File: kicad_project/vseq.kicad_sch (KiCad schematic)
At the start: 47 parts, among them J1 STM32_ADC_IN, J2 PROBE_INPUTS, U1 MCP6002, U2 MCP6002, U3 MCP6002, U4 MCP6002, U5 MCP6002

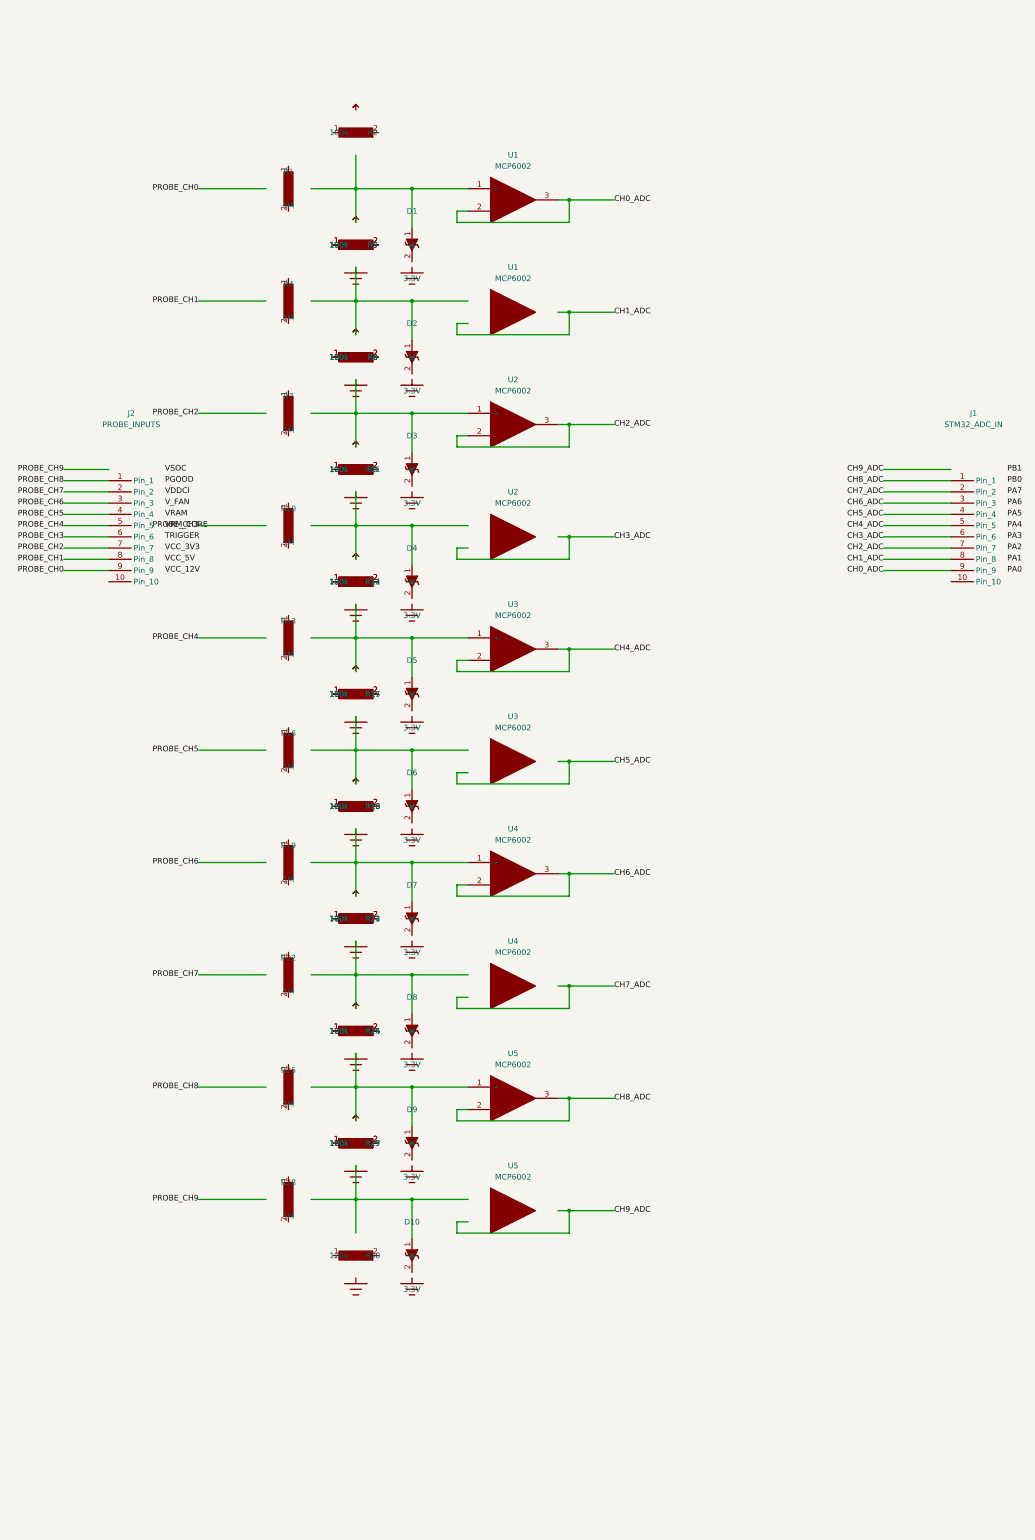
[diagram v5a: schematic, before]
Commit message: Complete rewrite: KiCad 7 valid schematic with TLV2371 op-amp buffer, correct polyline/pin syntax, valid PCB
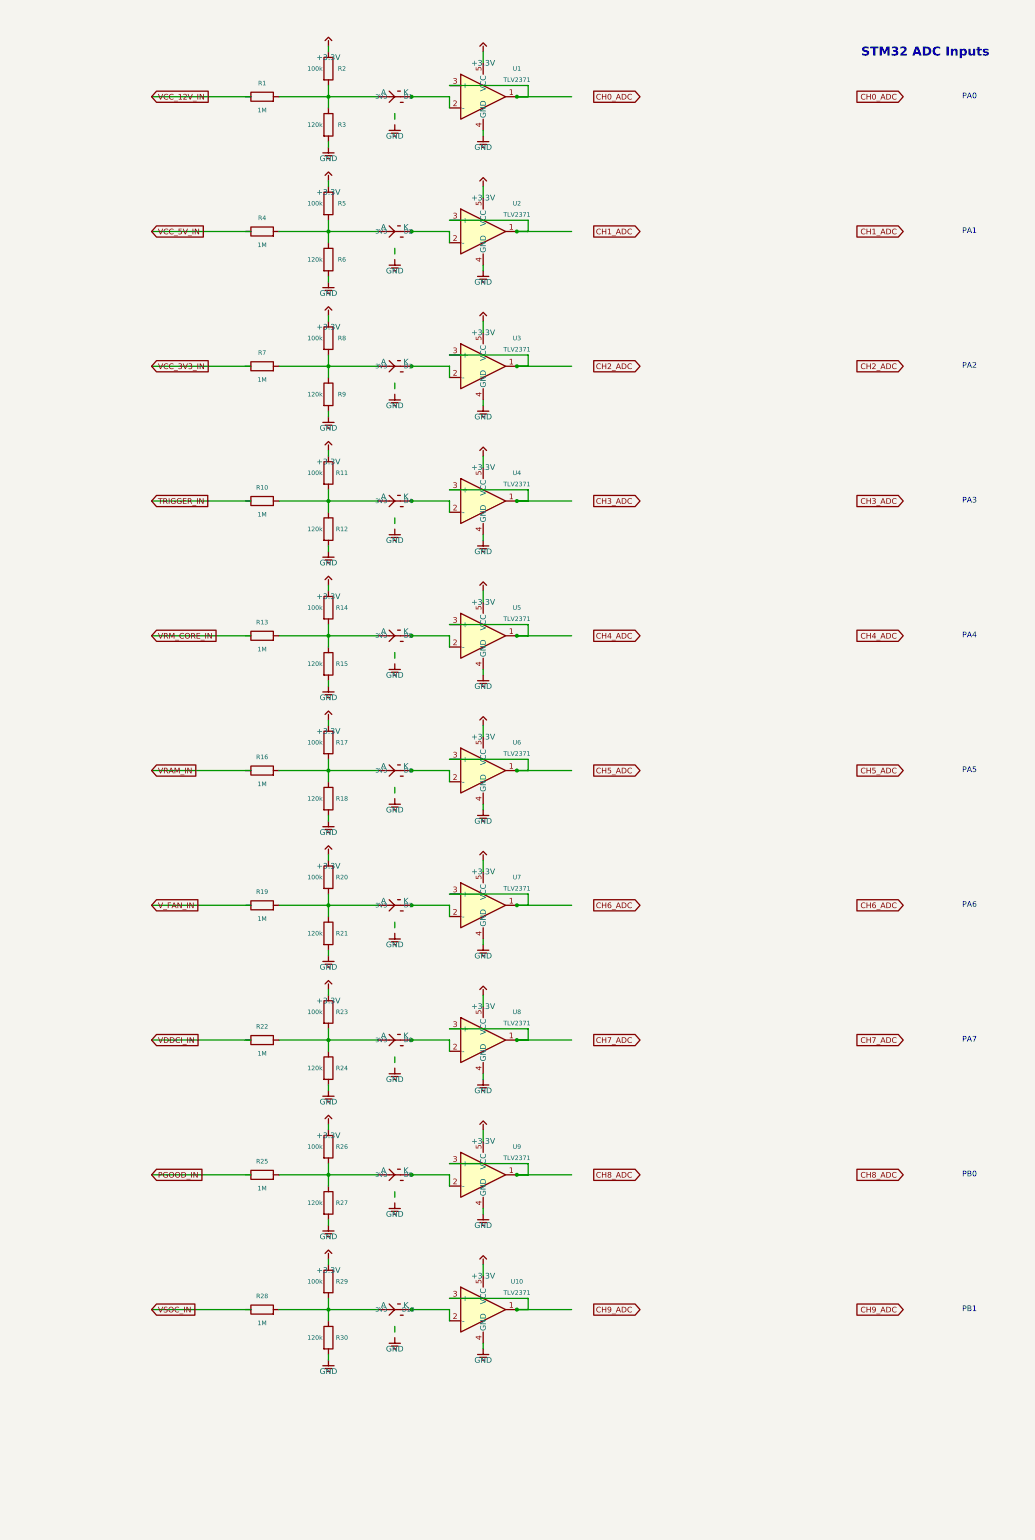
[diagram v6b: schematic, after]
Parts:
- removed J1: STM32_ADC_IN, Connector_PinHeader_2.54mm:PinHeader_1x10_P2.54mm_Vertical, symbol Connector:Conn_01x10_Male
- removed J2: PROBE_INPUTS, Connector_PinHeader_2.54mm:PinHeader_1x10_P2.54mm_Vertical, symbol Connector:Conn_01x10_Male
- removed U1, U2, U3, U4, U5: MCP6002, Package_SO:SOIC-8_3.9x4.9mm_P1.27mm, symbol Amplifier_Operational:MCP6002
- added U1, U10, U2, U3, U4, U5, U6, U7, U8, U9: TLV2371, Package_TO_SOT_THT:SOT-23-5, symbol Amplifier_Operational:TLV2371
- D1, D10, D2, D3, D4, D5, D6, D7, D8, D9: value 3.3V -> 3V3
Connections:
- net +3.3V: now also R11.1, R14.1, R17.1, R2.1, R20.1, R23.1, R26.1, R29.1, R5.1, R8.1, U1.5 (VCC), U10.5 (VCC), U2.5 (VCC), U3.5 (VCC), U4.5 (VCC), U5.5 (VCC), U6.5 (VCC), U7.5 (VCC), U8.5 (VCC), U9.5 (VCC); no longer D1.1 (K), D10.1 (K), D2.1 (K), D3.1 (K), D4.1 (K), D5.1 (K), D6.1 (K), D7.1 (K), D8.1 (K), D9.1 (K)
- net at R28.2: now also D10.2 (A), R29.2, R30.1
- net at R9.1: now also D3.2 (A), R7.2, R8.2; no longer R11.1
- net at R11.2: now also D4.2 (A), R10.2, R12.1; no longer R9.2
- net at R18.1: now also D6.2 (A), R16.2, R17.2; no longer R20.1
- net at R20.2: now also D7.2 (A), R19.2, R21.1; no longer R18.2
- net at R13.2: now also D5.2 (A), R14.2, R15.1
- net at R6.1: now also D2.2 (A), R4.2, R5.2; no longer R8.1
- net GND: now reaches R6.2
- net GND: now also R12.2, R15.2, R18.2, R21.2, R24.2, R27.2, R3.2, R30.2, R9.2, U1.4 (GND), U10.4 (GND), U2.4 (GND), U3.4 (GND), U4.4 (GND), U5.4 (GND), U6.4 (GND), U7.4 (GND), U8.4 (GND), U9.4 (GND); no longer R8.2
- net at R3.1: now also D1.2 (A), R1.2, R2.2; no longer R5.1
- net at R22.2: now also D8.2 (A), R23.2, R24.1
- net at D9.2 (A): now also R25.2, R26.2, R27.1
- new net: U1.1, U1.3 (+)
- new net: D1.1 (K), U1.2 (-)
- new net: D6.1 (K), U6.2 (-)
- new net: U10.1, U10.3 (+)
- new net: D10.1 (K), U10.2 (-)
- new net: U3.1, U3.3 (+)
- new net: D3.1 (K), U3.2 (-)
- new net: U7.1, U7.3 (+)
- new net: D7.1 (K), U7.2 (-)
- new net: U2.1, U2.3 (+)
- new net: D2.1 (K), U2.2 (-)
- new net: U8.1, U8.3 (+)
- new net: D8.1 (K), U8.2 (-)
- new net: U6.1, U6.3 (+)
- new net: U9.1, U9.3 (+)
- new net: D9.1 (K), U9.2 (-)
- new net: U5.1, U5.3 (+)
- new net: D5.1 (K), U5.2 (-)
- new net: D4.1 (K), U4.2 (-)
- new net: U4.1, U4.3 (+)
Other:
- note added: "PA0"
- note added: "PA1"
- note added: "PA2"
- note added: "PA3"
- note added: "PA4"
- note added: "PA5"
- note added: "PA6"
- note added: "PA7"
- note added: "PB0"
- note added: "PB1"
- note added: "STM32 ADC Inputs"
- title: VSeq 10-Channel Bipolar Voltage Analyzer -> VSeq 10-Channel Bipolar Voltage Analyser

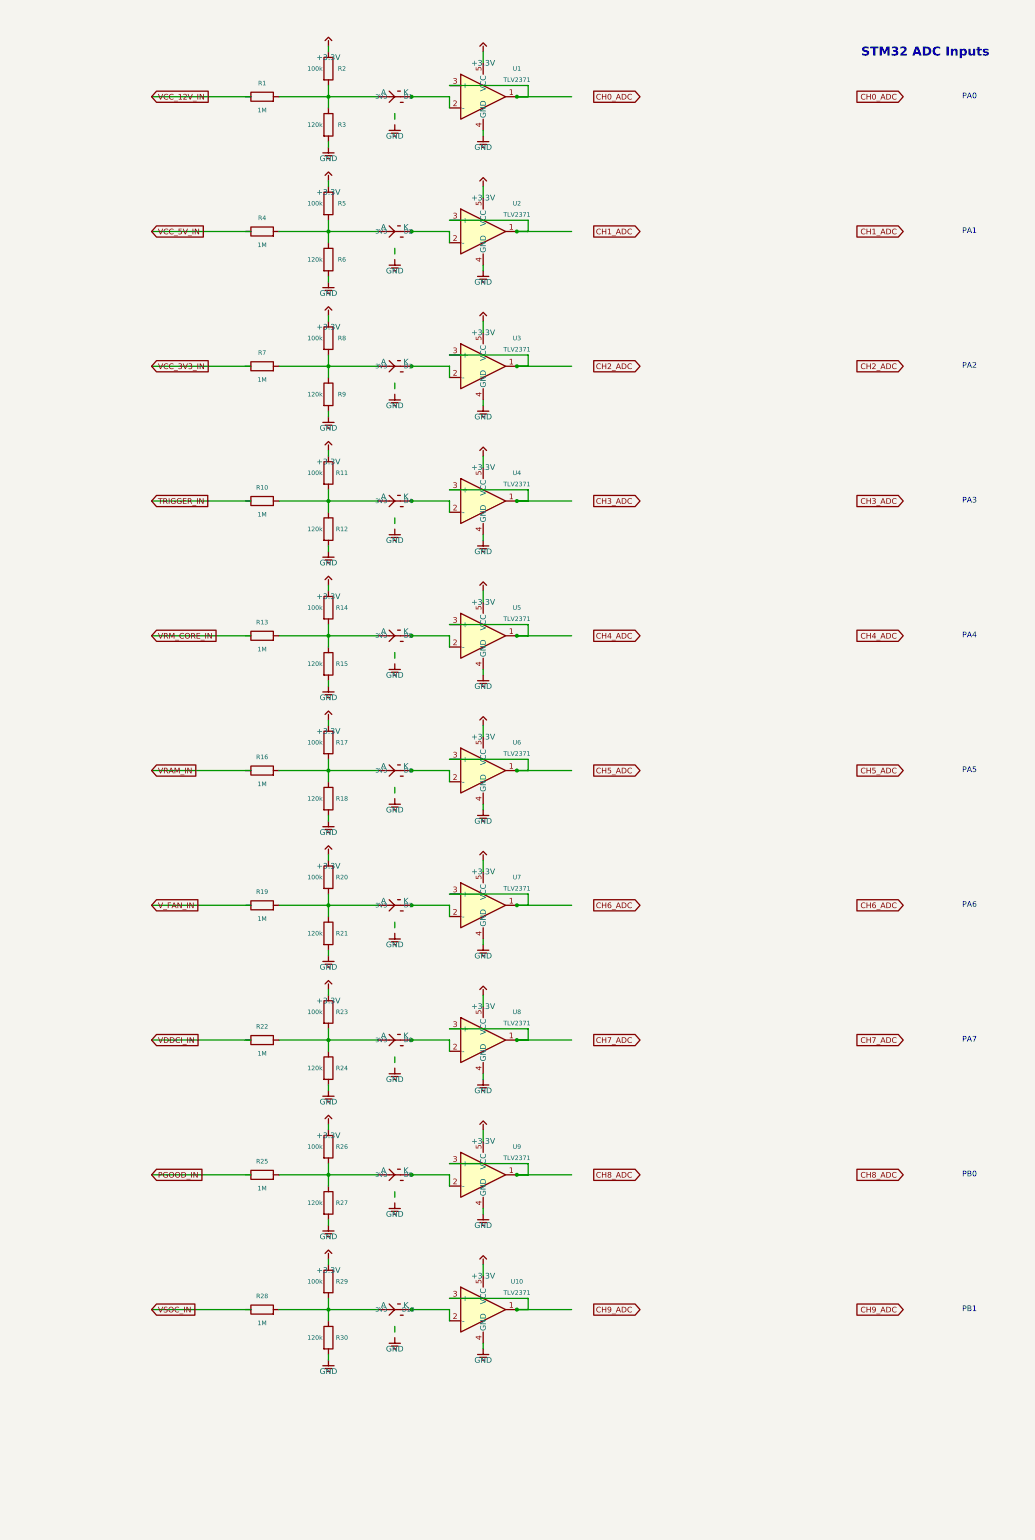
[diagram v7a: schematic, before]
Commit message: Fix: remove net_tie and smd_soldermask_margin, add proper global_label property, strip PCB setup to minimum
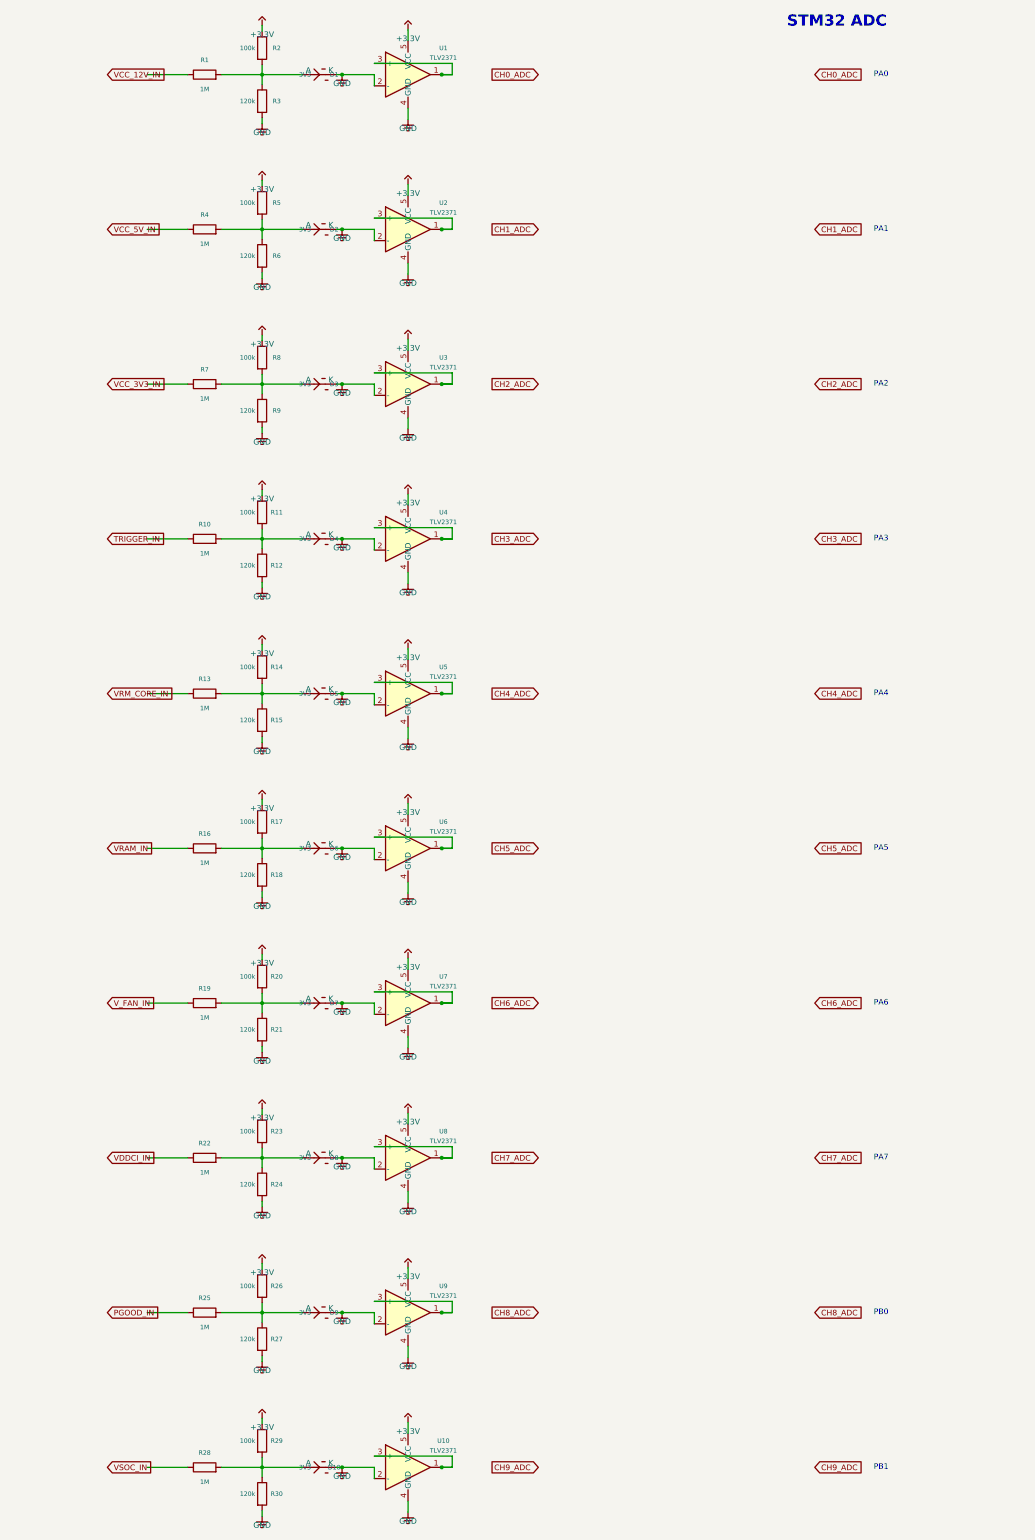
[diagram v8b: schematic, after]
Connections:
- net GND: now also D1.1 (K), D10.1 (K), D2.1 (K), D3.1 (K), D4.1 (K), D5.1 (K), D6.1 (K), D7.1 (K), D8.1 (K), D9.1 (K), U1.2 (-), U10.2 (-), U2.2 (-), U3.2 (-), U4.2 (-), U5.2 (-), U6.2 (-), U7.2 (-), U8.2 (-), U9.2 (-)
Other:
- note added: "STM32 ADC"
- note removed: "STM32 ADC Inputs"
